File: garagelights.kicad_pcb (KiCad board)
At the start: 2 copper layers, 69.8 x 76.2 mm, 40 parts, among them J1 Conn_01x04, J2 Conn_01x06, J3 Screw_Terminal_01x01, J4 Screw_Terminal_01x01, Q1 ZVN4206AV, Q2 ZVN4206AV, Q3 ZVN4206AV, U1 NE555P, U2 NE555P, U3 4013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

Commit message: Moved the connectors to the bottom side
Makes the mechanical design easier. Also some tweaks to reduce
inductance on the +5V net.
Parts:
- J1, J2: moved to B.Cu
- moved J1 4.95 mm to (167.6, 91.4), turned to 90 degrees
- moved C7 3.18 mm to (145.4, 122.2)
- moved J2 0.61 mm to (157.5, 122.2), turned to -90 degrees
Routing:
- net Net-(J1-Pin_3): track 91.3 -> 84.0 mm
- net Net-(J1-Pin_2): track 10.6 -> 15.3 mm
- net Net-(J2-Pin_4): track 9.75 -> 9.12 mm
- net Net-(J2-Pin_3): track 11.9 -> 11.3 mm
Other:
- board text added: "+12V"
- board text added: "+5V"
- board text added: "ECHO"
- board text added: "GND"
- board text added: "GREEN"
- board text added: "HC-SR04"
- board text added: "N/C"
- board text added: "PING"
- board text added: "RED"
- board text added: "~{GREEN}"
- board text added: "~{RED}"
- board text added: "~{YELLOW}"

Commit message: Change "PING" to "TRIG" to better match HC-SR04 nomenclature.
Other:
- board text added: "TRIG"
- board text removed: "PING"
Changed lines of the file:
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@@
 		)
 	)
-	(gr_text "PING"
+	(gr_text "TRIG"
 		(at 165.735 88.9 90)
 		(layer "F.SilkS")
@@
 		)
 	)
-	(gr_text "PING"
+	(gr_text "TRIG"
 		(at 164.465 88.9 270)
 		(layer "B.SilkS")

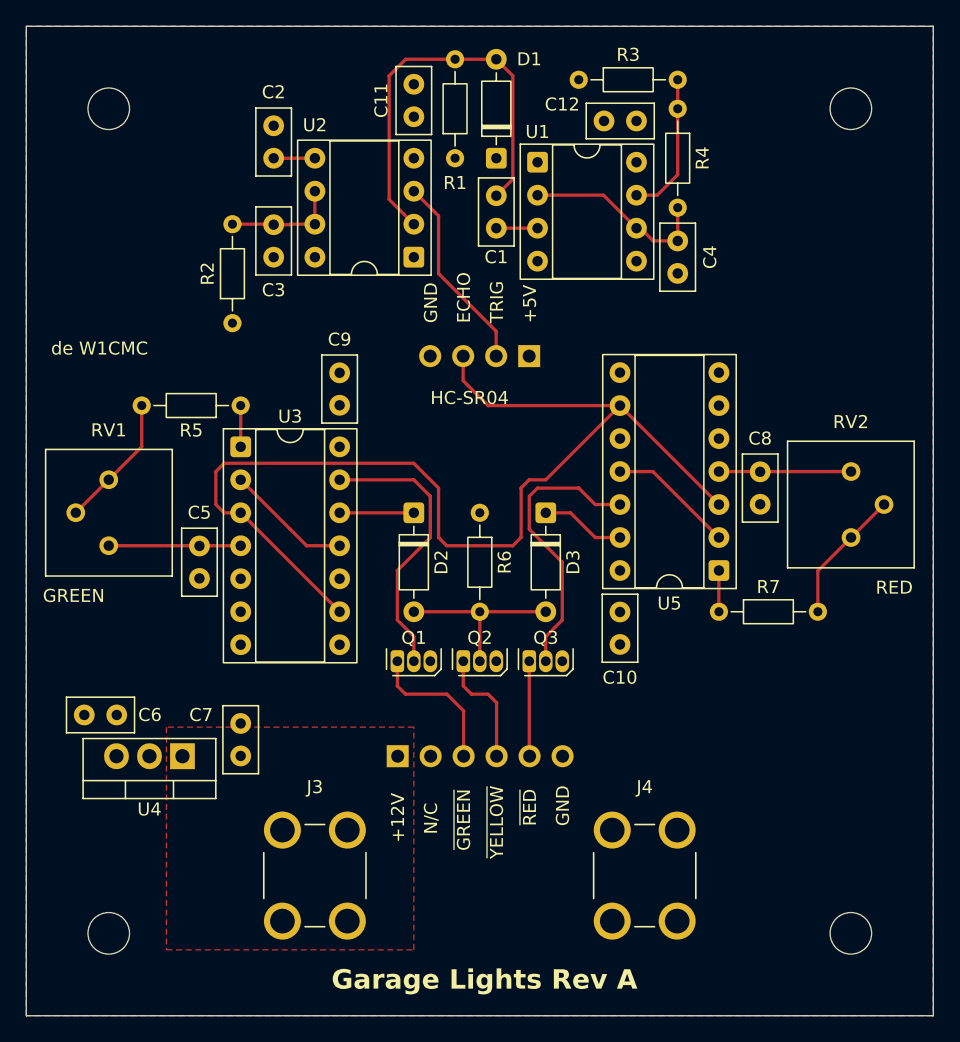
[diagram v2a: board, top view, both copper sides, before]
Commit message: Spec Samtec connectors for the socket headers.
Also more fussing with position and text.
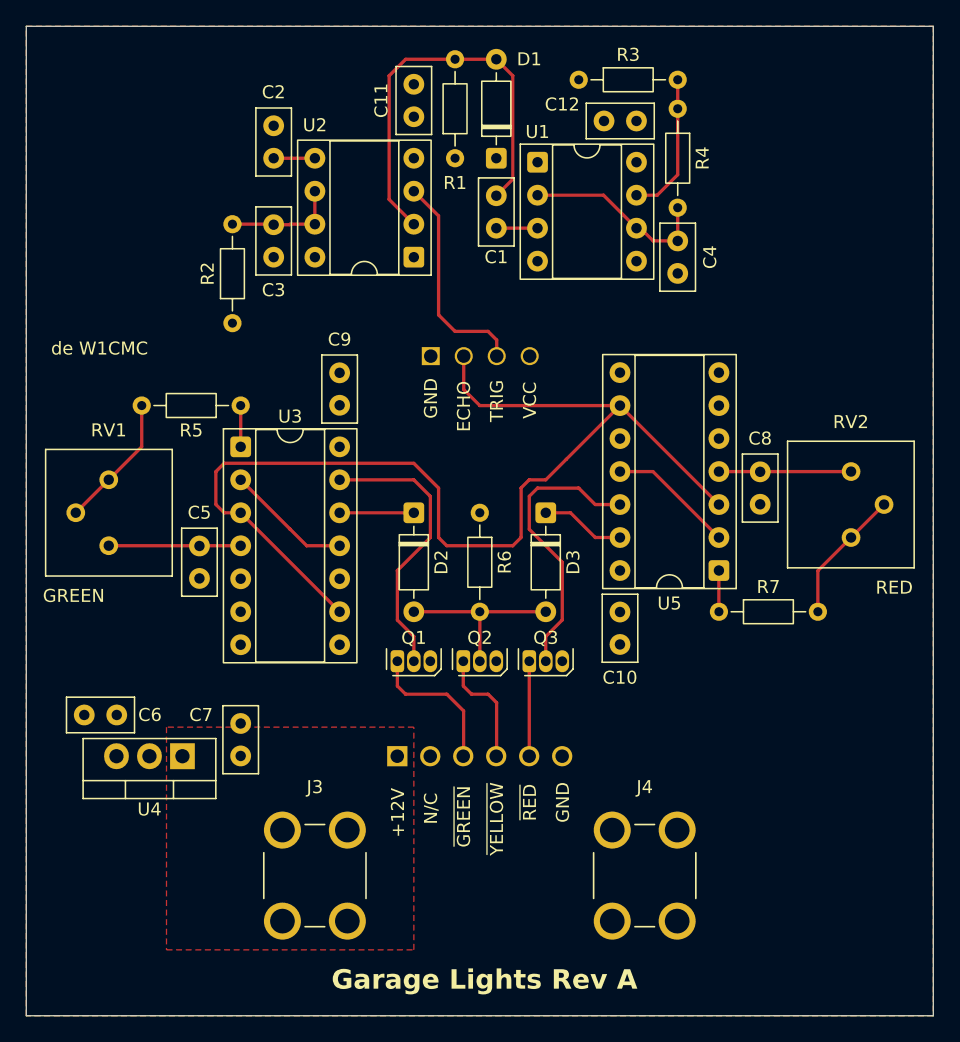
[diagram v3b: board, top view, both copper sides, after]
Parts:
- removed REF** (x4): MountingHole_3.2mm_M3, MountingHole:MountingHole_3.2mm_M3
- J1: value Conn_01x04 -> Samtec SSW-104-03-F-S-RA; footprint Connector_PinSocket_2.54mm:PinSocket_1x04_P2.54mm_Vertical -> Library:SAMTEC_SSW-104-03-F-S-RA
- J2: value Conn_01x06 -> Samtec SSW-106-01-L-S; footprint Connector_PinSocket_2.54mm:PinSocket_1x06_P2.54mm_Vertical -> Library:SAMTEC_SSW-106-01-X-S
- moved J1 7.58 mm to (160.1, 91.4), turned to 180 degrees
- moved J2 6.32 mm to (163.8, 122.2), turned to 0 degrees
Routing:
- net Net-(J1-Pin_2): track 15.3 -> 16.8 mm
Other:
- board text added: "VCC"
- board text removed: "+5V"
- board text removed: "HC-SR04"

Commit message: Put the mounting holes into the schematic.
So that we don't keep losing them when we update the layout from
the schematic.
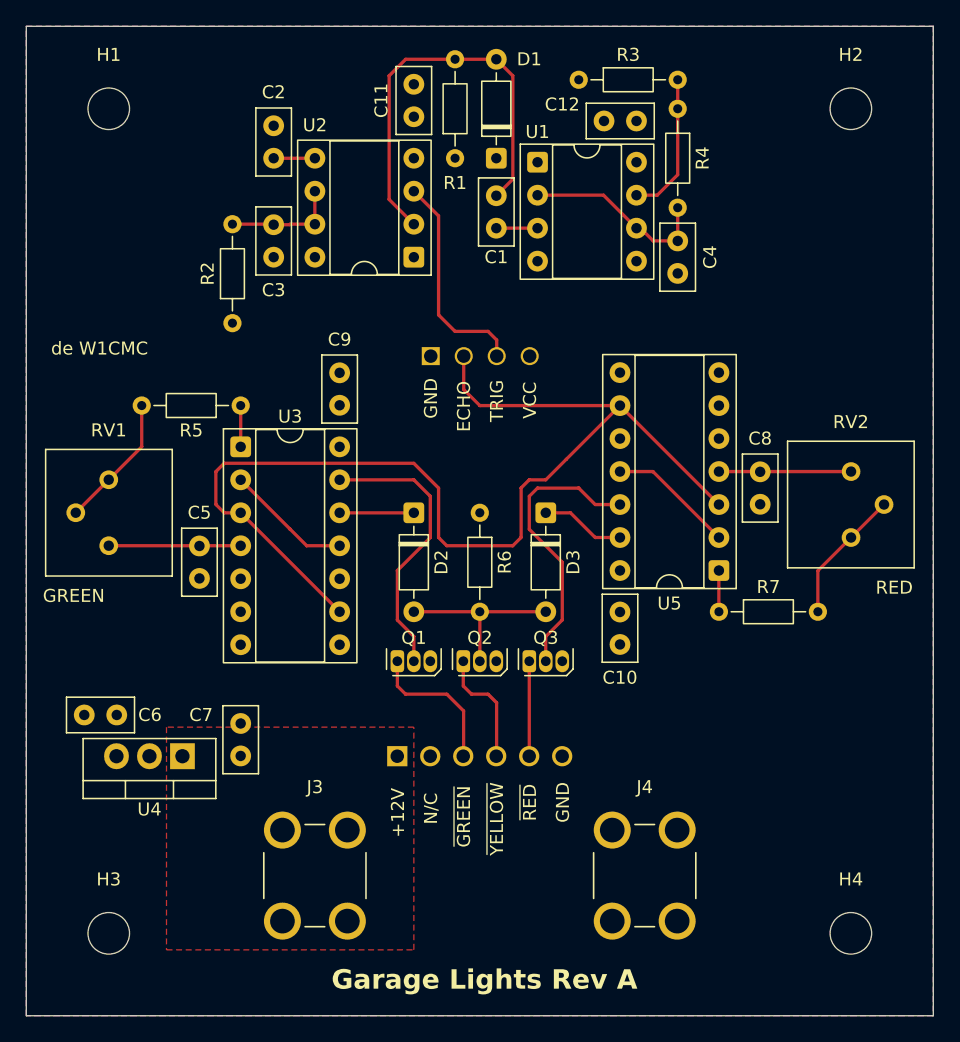
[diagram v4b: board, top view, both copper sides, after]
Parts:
- added H1: MountingHole, MountingHole:MountingHole_3.2mm_M3, F.Cu at (135.3, 72.4)
- added H2: MountingHole, MountingHole:MountingHole_3.2mm_M3, F.Cu at (192.4, 72.4)
- added H3: MountingHole, MountingHole:MountingHole_3.2mm_M3, F.Cu at (135.3, 135.9)
- added H4: MountingHole, MountingHole:MountingHole_3.2mm_M3, F.Cu at (192.4, 135.9)

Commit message: Rev A: as submitted to Osh Park order #fmnAZ4b4
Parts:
- J2: value Samtec SSW-106-01-L-S -> Molex 901361106; footprint Library:SAMTEC_SSW-106-01-X-S -> Library:CONN_SDA-90136_V_06_MOL
- moved D1 8.25 mm to (161.9, 68.6), turned to -90 degrees
- moved R1 8.25 mm to (165.1, 68.6), turned to -90 degrees
- moved J2 6.32 mm to (157.5, 122.2), turned to 180 degrees
- moved J3 3.12 mm to (148.0, 131.4)
- moved J4 2.92 mm to (179.4, 131.4)
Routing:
- net Net-(D1-A): track 32.6 -> 14.0 mm
- net Net-(J1-Pin_2): track 16.8 -> 21.0 mm

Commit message: Changed the timing capacitors: 1 uF ceramic C0G isn't a thing.
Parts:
- C5: value 1 uF -> 0.1
- R5, RV1: value 10k -> 100k
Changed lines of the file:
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@@
 			)
 		)
-		(property "Value" "1 uF"
+		(property "Value" "0.1"
 			(at 1.25 2.5 90)
 			(layer "F.Fab")
@@
 			)
 		)
-		(property "Value" "10k"
+		(property "Value" "100k"
 			(at 3.81 1.92 0)
 			(layer "F.Fab")
@@
 			)
 		)
-		(property "Value" "10k"
+		(property "Value" "100k"
 			(at -0.015 3.475 0)
 			(layer "F.Fab")

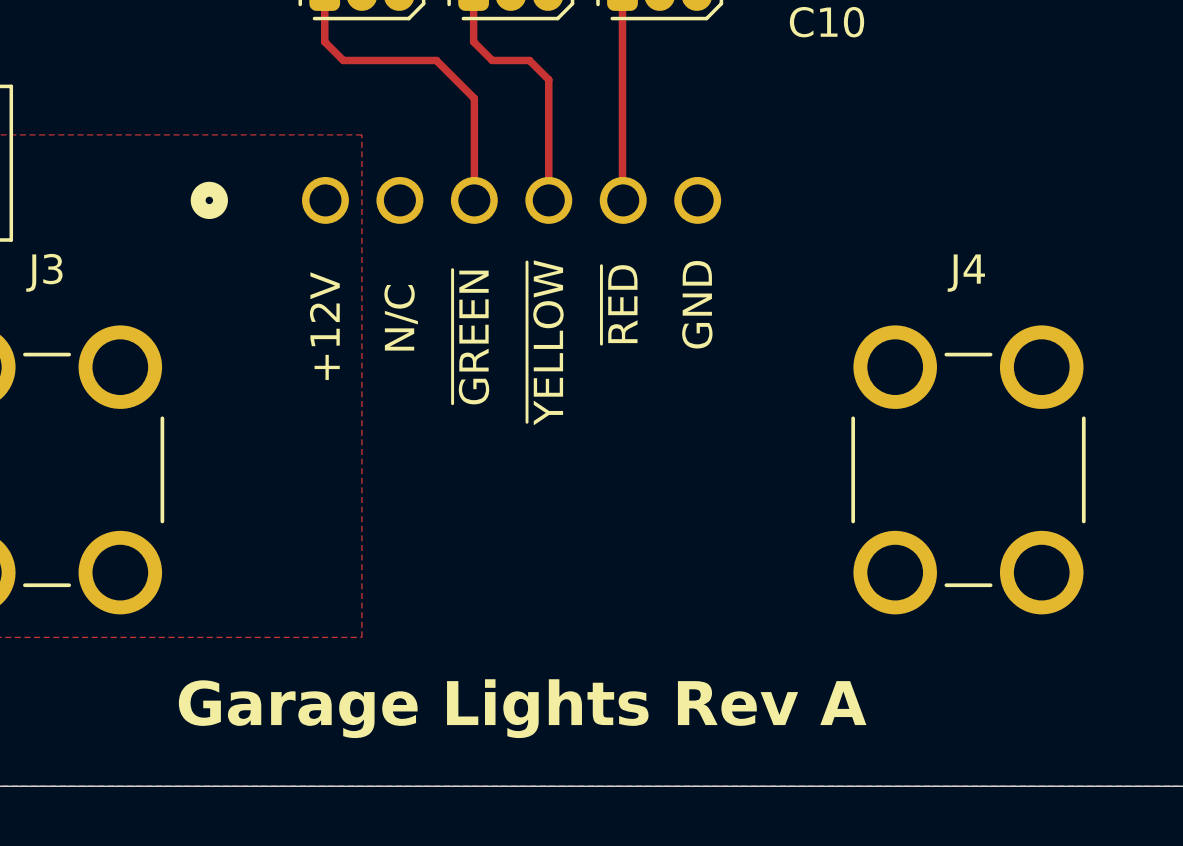
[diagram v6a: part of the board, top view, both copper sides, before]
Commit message: Update to KiCAD 10.0, replace J2 with 5-pin
J2 was 6-pin, but the ground pin was superfluous. The light tower
is switched on the low side, so there is no ground conductor.
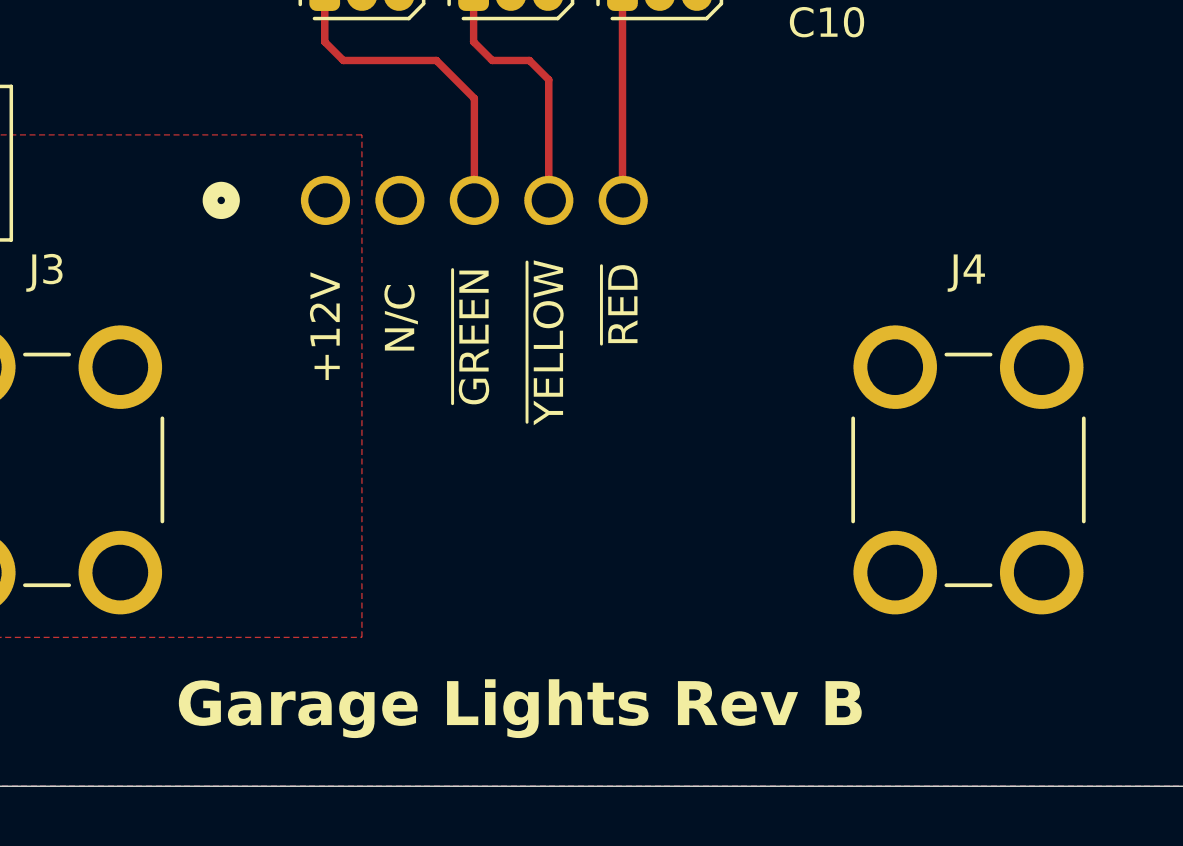
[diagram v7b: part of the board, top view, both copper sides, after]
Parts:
- J2: value Molex 901361106 -> Molex 705430004; footprint Library:CONN_SDA-90136_V_06_MOL -> Library:CONN_SDA-70543-xxxx_05_MOL
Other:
- board text added: "Garage Lights Rev B"
- board text removed: "Garage Lights Rev A"

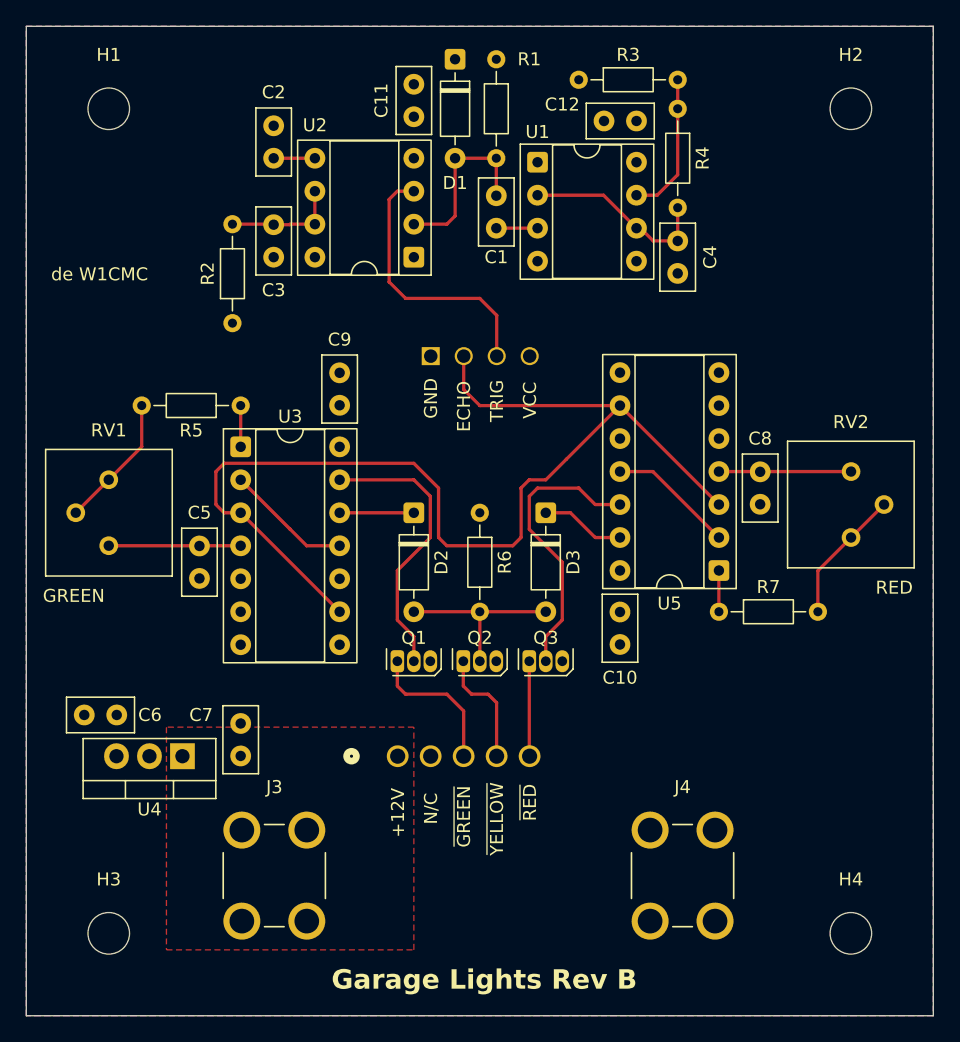
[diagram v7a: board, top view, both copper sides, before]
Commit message: Fixed a couple of boo-boos:
1. Bigger resistors
2. Correct footprint for pots
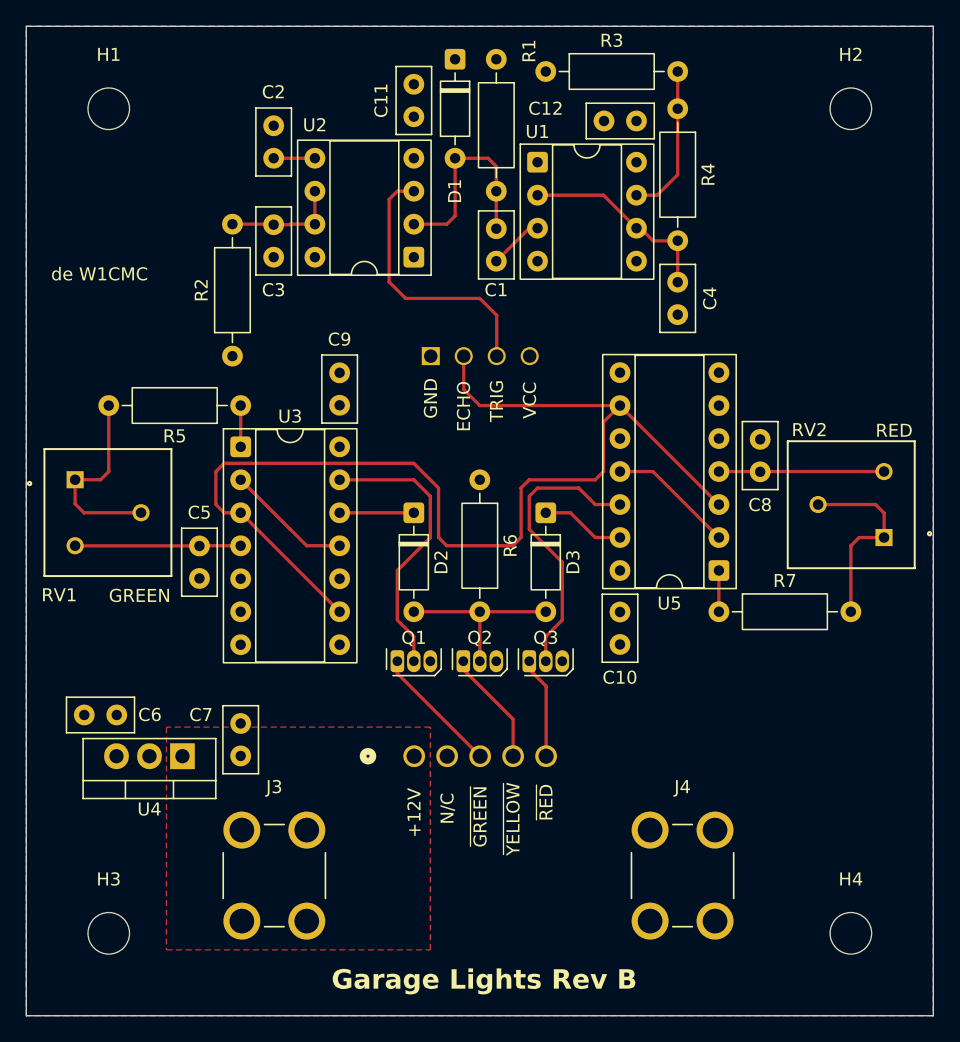
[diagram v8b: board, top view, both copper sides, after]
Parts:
- R1, R2, R3, R4, R5, R6, R7: footprint Resistor_THT:R_Axial_DIN0204_L3.6mm_D1.6mm_P7.62mm_Horizontal -> Resistor_THT:R_Axial_DIN0207_L6.3mm_D2.5mm_P10.16mm_Horizontal
- RV1, RV2: footprint Potentiometer_THT:Potentiometer_Bourns_3386P_Vertical -> Library:POT_3386F
- moved C4 3.18 mm to (179.1, 85.7)
- moved R3 2.62 mm to (168.9, 69.5)
- moved RV1 2.59 mm to (132.7, 101.0), turned to -90 degrees
- moved RV2 2.54 mm to (195.0, 105.4), turned to 90 degrees
- moved C1 2.54 mm to (165.1, 84.1)
- moved R2 2.54 mm to (144.8, 91.4)
- moved R6 2.54 mm to (163.8, 101.0)
- moved J2 1.27 mm to (158.8, 122.2)
- turned C8 to 90 degrees
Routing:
- net Net-(R5-Pad2): track 10.4 -> 15.2 mm
- net Net-(R7-Pad2): track 10.4 -> 15.1 mm
- net Net-(U3A-R): track 10.2 -> 12.8 mm
- net Net-(U5A-R): track 10.2 -> 12.7 mm
- net Net-(J1-Pin_3): track 84.3 -> 86.6 mm
- net Net-(D1-A): track 14.0 -> 16.1 mm
- net Net-(J2-Pin_3): track 11.3 -> 9.96 mm
- net Net-(U1-Q): track 3.18 -> 4.23 mm
- net Net-(U1-THR): track 14.8 -> 15.4 mm
- net Net-(J2-Pin_5): track 7.33 -> 7.85 mm
